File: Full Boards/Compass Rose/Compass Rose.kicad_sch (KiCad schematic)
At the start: 248 parts, among them J1 Program Header, J3 Optional Bond, Q1 BSS314PE, Q2 DMN6075S, Q3 BSS314PE, Q4 DMN6075S, Q5 BSS314PE, Q6 DMN6075S, SW1 Boot, SW2 Reset, SW3 CTS_219-2MSTR

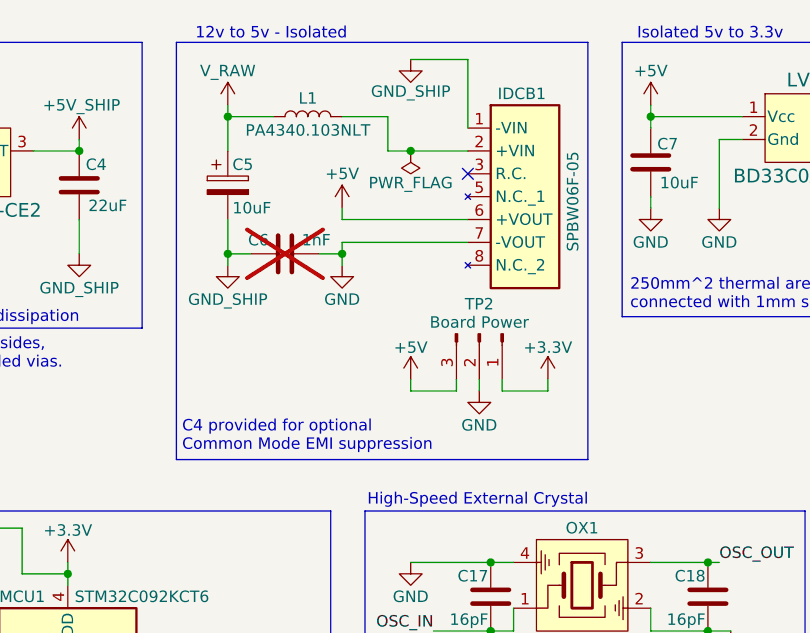
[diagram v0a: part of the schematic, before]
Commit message: Added ID, license, and common mode surge supression instructions to silkscreen
Signed-off-by: digimer <digital.mermaid@gmail.com>
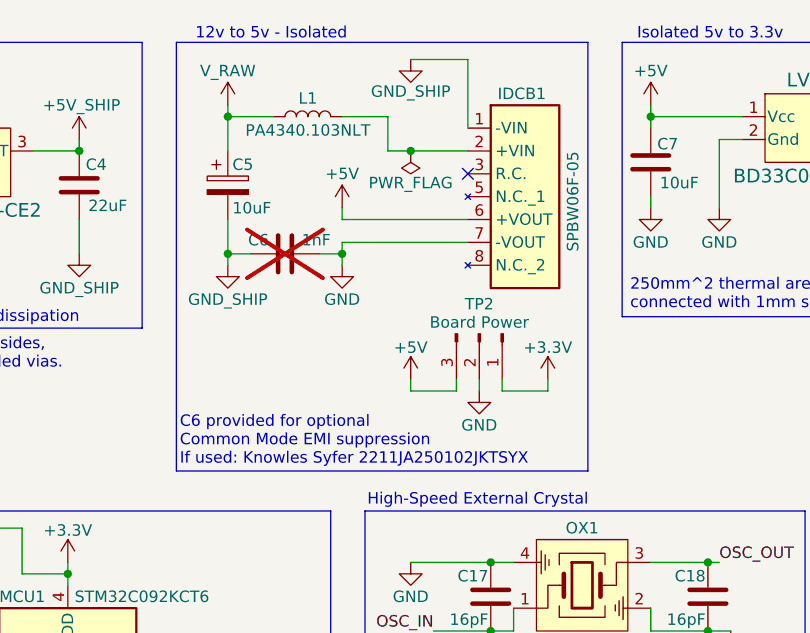
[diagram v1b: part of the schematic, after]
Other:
- note added: "C6 provided for optional Common Mode EMI suppression If used: Knowles Syfer 2211JA250102JKTSYX"
- note removed: "C4 provided for optional Common Mode EMI suppression"
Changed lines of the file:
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@@
 	(rectangle
 		(start 177.165 15.875)
-		(end 222.885 62.23)
+		(end 222.885 63.5)
 		(stroke
 			(width 0)
@@
 		)
 	)
-	(text "C4 provided for optional \nCommon Mode EMI suppression"
-		(exclude_from_sim no)
-		(at 177.8 57.912 0)
-		(effects
-			(font
+	(text "C6 provided for optional \nCommon Mode EMI suppression\nIf used: Knowles Syfer 2211JA250102JKTSYX"
+		(exclude_from_sim no)
+		(at 177.546 57.404 0)
+		(effects
+			(font

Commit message: Added missing fiducial footprints.
Signed-off-by: digimer <digital.mermaid@gmail.com>
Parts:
- FID1, FID2, FID3: footprint (none) -> Fiducial:Fiducial_0.5mm_Mask1.5mm
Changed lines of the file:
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@@
 			)
 		)
-		(property "Footprint" ""
+		(property "Footprint" "Fiducial:Fiducial_0.5mm_Mask1.5mm"
 			(at 287.02 231.14 0)
 			(hide yes)
@@
 			)
 		)
-		(property "Footprint" ""
+		(property "Footprint" "Fiducial:Fiducial_0.5mm_Mask1.5mm"
 			(at 491.49 29.21 0)
 			(hide yes)
@@
 			)
 		)
-		(property "Footprint" ""
+		(property "Footprint" "Fiducial:Fiducial_0.5mm_Mask1.5mm"
 			(at 492.76 243.84 0)
 			(hide yes)

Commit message: Updated PCB and schematic to pickup new footprint attributes.
Signed-off-by: digimer <digital.mermaid@gmail.com>
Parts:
- C6: Part Knowles Syfer 2211JA250102JKTSYX -> (none)
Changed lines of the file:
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@@
-			)
-		)
-		(property "Part" "Knowles Syfer 2211JA250102JKTSYX"
-			(at 189.23 39.37 90)
-			(hide yes)
-			(show_name no)
-			(do_not_autoplace no)
-			(effects
-				(font
-					(size 1.27 1.27)
-				)
 			)
 		)

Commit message: Fixed a mismatch footprint for the Rohm BD4xx5S part.
Signed-off-by: digimer <digital.mermaid@gmail.com>
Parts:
- LVR1: footprint mr-stuff:Rohm BD4xxS5-C -> mr-stuff:Rohm BD4xxS5 TO252-3; symbol mr-parts:Rohm BD450S5FP-CE2 -> mr-parts:Rohm BD450S5WFP-CE2; Part Rohm BD450S5FP-CE2 -> Rohm BD450S5WFP-CE2
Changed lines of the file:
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@@
 	)
 	(symbol
-		(lib_id "mr-parts:Rohm BD450S5FP-CE2")
+		(lib_id "mr-parts:Rohm BD450S5WFP-CE2")
 		(at 153.67 29.21 0)
 		(unit 1)
@@
 			)
 		)
-		(property "Footprint" "mr-stuff:Rohm BD4xxS5-C"
+		(property "Footprint" "mr-stuff:Rohm BD4xxS5 TO252-3"
 			(at 153.67 43.688 0)
 			(hide yes)
@@
 			)
 		)
-		(property "Description" "Linear Voltage Regulator IC Positive Fixed 1 Output 500mA TO-252-5"
+		(property "Description" "Linear Voltage Regulator IC Positive Fixed 1 Output 500mA TO-252-3"
 			(at 153.67 39.37 0)
 			(hide yes)
@@
 			)
 		)
-		(property "Part" "Rohm BD450S5FP-CE2"
+		(property "Part" "Rohm BD450S5WFP-CE2"
 			(at 153.67 37.338 0)
 			(hide yes)

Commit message: Fixing the last commit's fix, which didn't need fixing. (Thanks, Digikey...)
Signed-off-by: digimer <digital.mermaid@gmail.com>
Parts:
- LVR1: symbol mr-parts:Rohm BD450S5WFP-CE2 -> mr-parts:Rohm BD450S5FP-CE2; Part Rohm BD450S5WFP-CE2 -> Rohm BD450S5FP-CE2
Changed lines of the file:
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@@
 	)
 	(symbol
-		(lib_id "mr-parts:Rohm BD450S5WFP-CE2")
+		(lib_id "mr-parts:Rohm BD450S5FP-CE2")
 		(at 153.67 29.21 0)
 		(unit 1)
@@
 			)
 		)
-		(property "Part" "Rohm BD450S5WFP-CE2"
+		(property "Part" "Rohm BD450S5FP-CE2"
 			(at 153.67 37.338 0)
 			(hide yes)
